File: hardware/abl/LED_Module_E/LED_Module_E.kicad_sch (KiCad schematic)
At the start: 90 parts, among them J1 SFW20S-2STE1LF, J3 009159008603906, Q1 Si3456DDV, Q11 Si3456DDV, Q12 Si3456DDV, Q2 Si3456DDV, Q3 Si3456DDV, Q4 Si3456DDV, Q5 Si3456DDV, Q6 Si3456DDV, Q7 Si3456DDV, Q8 Si3456DDV, U1 TMP1075DGK, U2 74HC245, U3 24AA025UIDT-I/OT

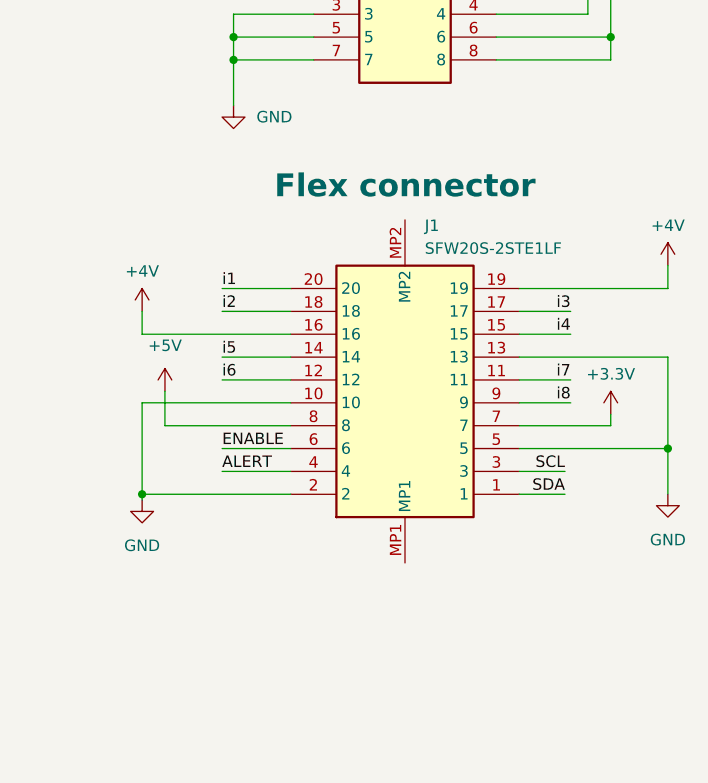
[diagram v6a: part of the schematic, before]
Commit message: Fix orientation of the flex connector.
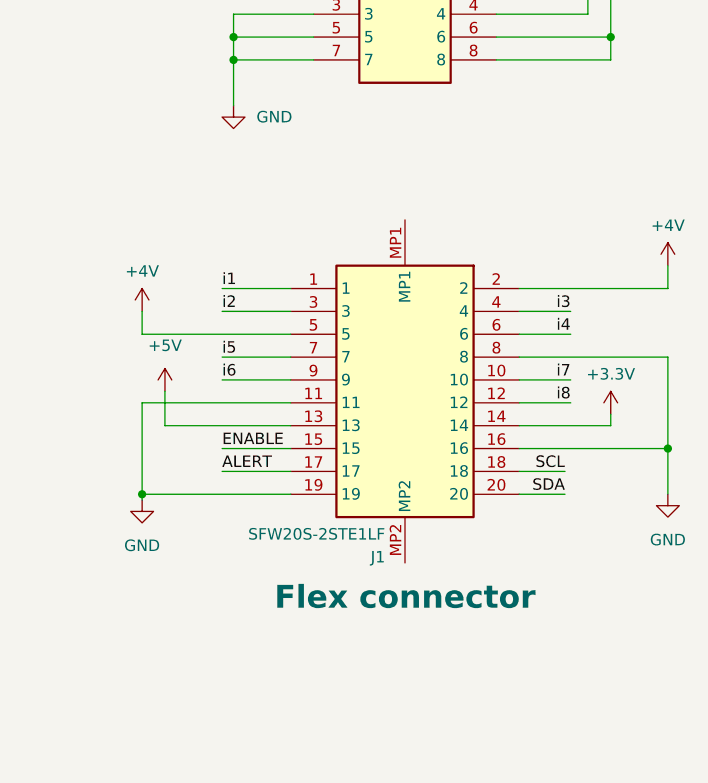
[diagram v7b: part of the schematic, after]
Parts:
- J1: footprint SFW20S2STE1LF -> Own footprints:SFW20S2STE1LF_Own
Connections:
- net +3.3V: now also J1.14; no longer J1.7
- net +4V: now also J1.2, J1.5; no longer J1.16, J1.19
- net +5V: now also J1.13; no longer J1.8
- net ALERT: now also J1.17; no longer J1.4
- net ENABLE: now also J1.15; no longer J1.6
- net GND: now also J1.11, J1.16, J1.19, J1.8; no longer J1.10, J1.13, J1.2, J1.5
- net SCL: now also J1.18; no longer J1.3
- net SDA: now also J1.20; no longer J1.1
- net i1: now also J1.1; no longer J1.20
- net i2: now also J1.3; no longer J1.18
- net i3: now also J1.4; no longer J1.17
- net i4: now also J1.6; no longer J1.15
- net i5: now also J1.7; no longer J1.14
- net i6: now also J1.9; no longer J1.12
- net i7: now also J1.10; no longer J1.11
- net i8: now also J1.12; no longer J1.9
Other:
- moved on the sheet: J1
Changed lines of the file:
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@@
 	(symbol
 		(lib_id "SFW20S-2STE1LF:SFW20S-2STE1LF")
-		(at 246.38 154.94 90)
+		(at 246.38 116.84 270)
 		(unit 1)
 		(exclude_from_sim no)
@@
 		(dnp no)
 		(property "Reference" "J1"
-			(at 248.5741 117.475 90)
+			(at 244.1859 154.305 90)
 			(effects
 				(font
@@
 		)
 		(property "Value" "SFW20S-2STE1LF"
-			(at 248.5741 120.015 90)
+			(at 244.1859 151.765 90)
 			(effects
 				(font
@@
 			)
 		)
-		(property "Footprint" "SFW20S2STE1LF"
-			(at 336.22 120.65 0)
+		(property "Footprint" "Own footprints:SFW20S2STE1LF_Own"
+			(at 156.54 151.13 0)
 			(effects
 				(font
@@
 		)
 		(property "Datasheet" "https://cdn.amphenol-cs.com/media/wysiwyg/files/drawing/10172832.pdf"
-			(at 436.22 120.65 0)
+			(at 56.54 151.13 0)
 			(effects
 				(font
@@
 		)
 		(property "Description" "1.00mm Flex Connector, SFW Straight series, 20 Position, Top Entry Surface Mount, ZIF"
-			(at 246.38 154.94 0)
+			(at 246.38 116.84 0)
 			(effects
 				(font
@@
 		)
 		(property "Manufacturer_Name" "Amphenol Communications Solutions"
-			(at 936.22 120.65 0)
+			(at -443.46 151.13 0)
 			(effects
 				(font
@@
 		)
 		(property "Manufacturer_Part_Number" "SFW20S-2STE1LF"
-			(at 1036.22 120.65 0)
+			(at -543.46 151.13 0)
 			(effects
 				(font
@@
 		)
 		(property "LCSC Part #" "C5407823"
-			(at 246.38 154.94 0)
+			(at 246.38 116.84 0)
 			(effects
 				(font
@@
 		)
 		(property "Purpose" "Flex connector"
-			(at 246.38 113.03 90)
+			(at 246.38 158.75 90)
 			(effects
 				(font
@@
 		)
 		(property "Note" ""
-			(at 246.38 154.94 0)
+			(at 246.38 116.84 0)
 			(effects
 				(font

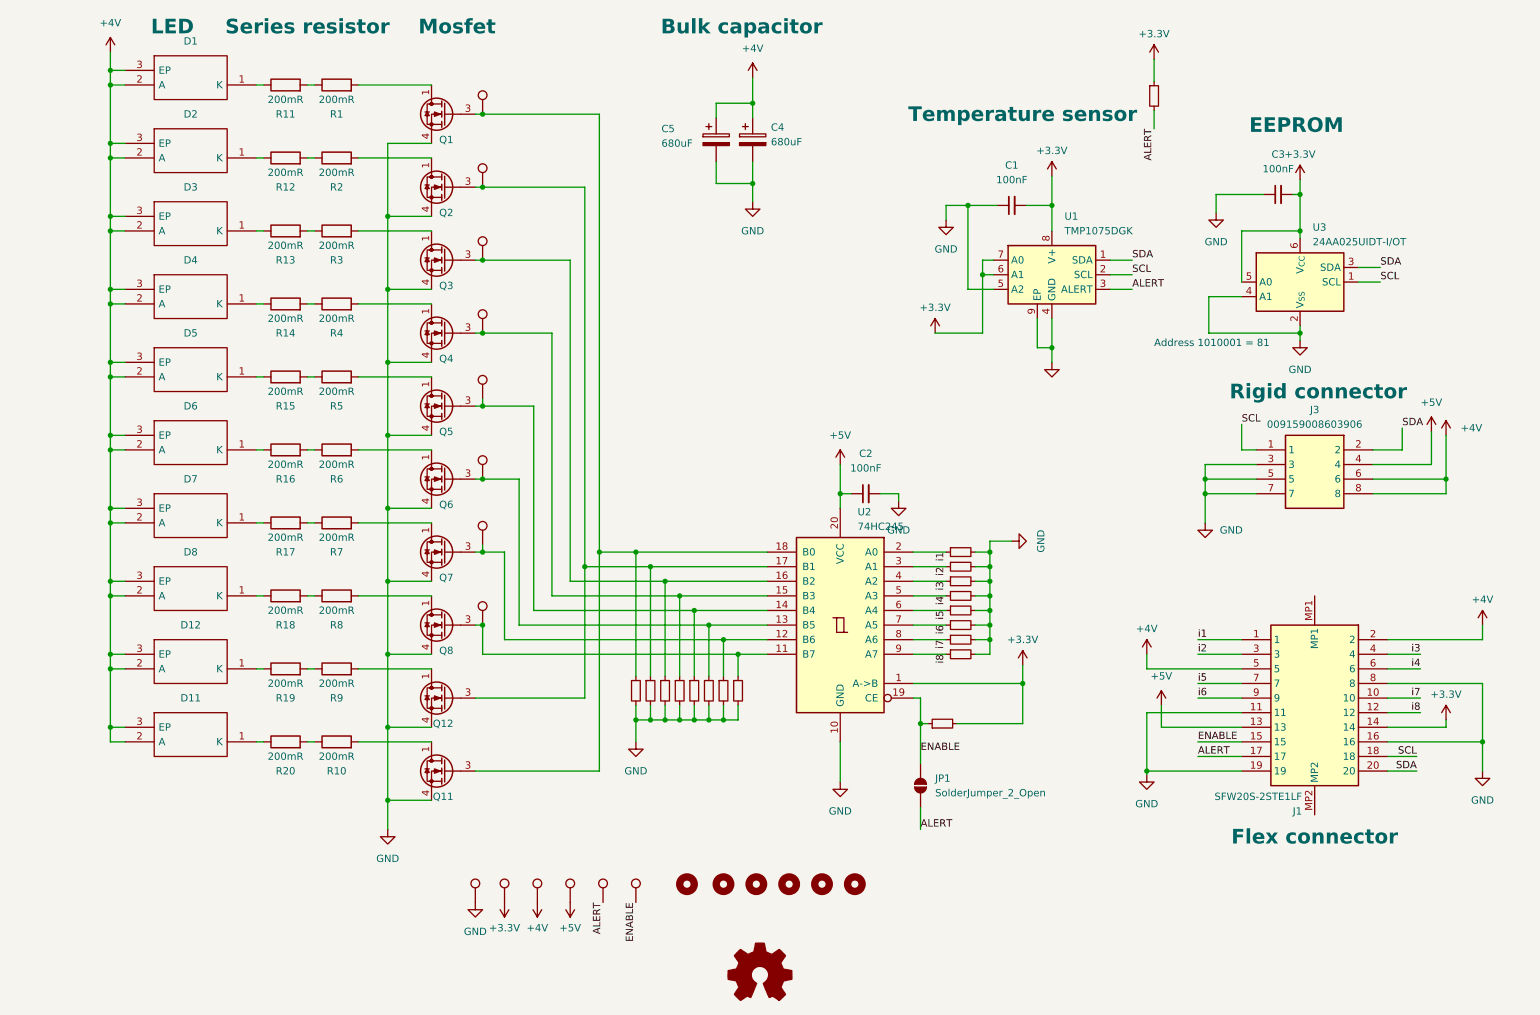
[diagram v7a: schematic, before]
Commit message: Add small copper PCB that only contains LEDs and temperature sensor.
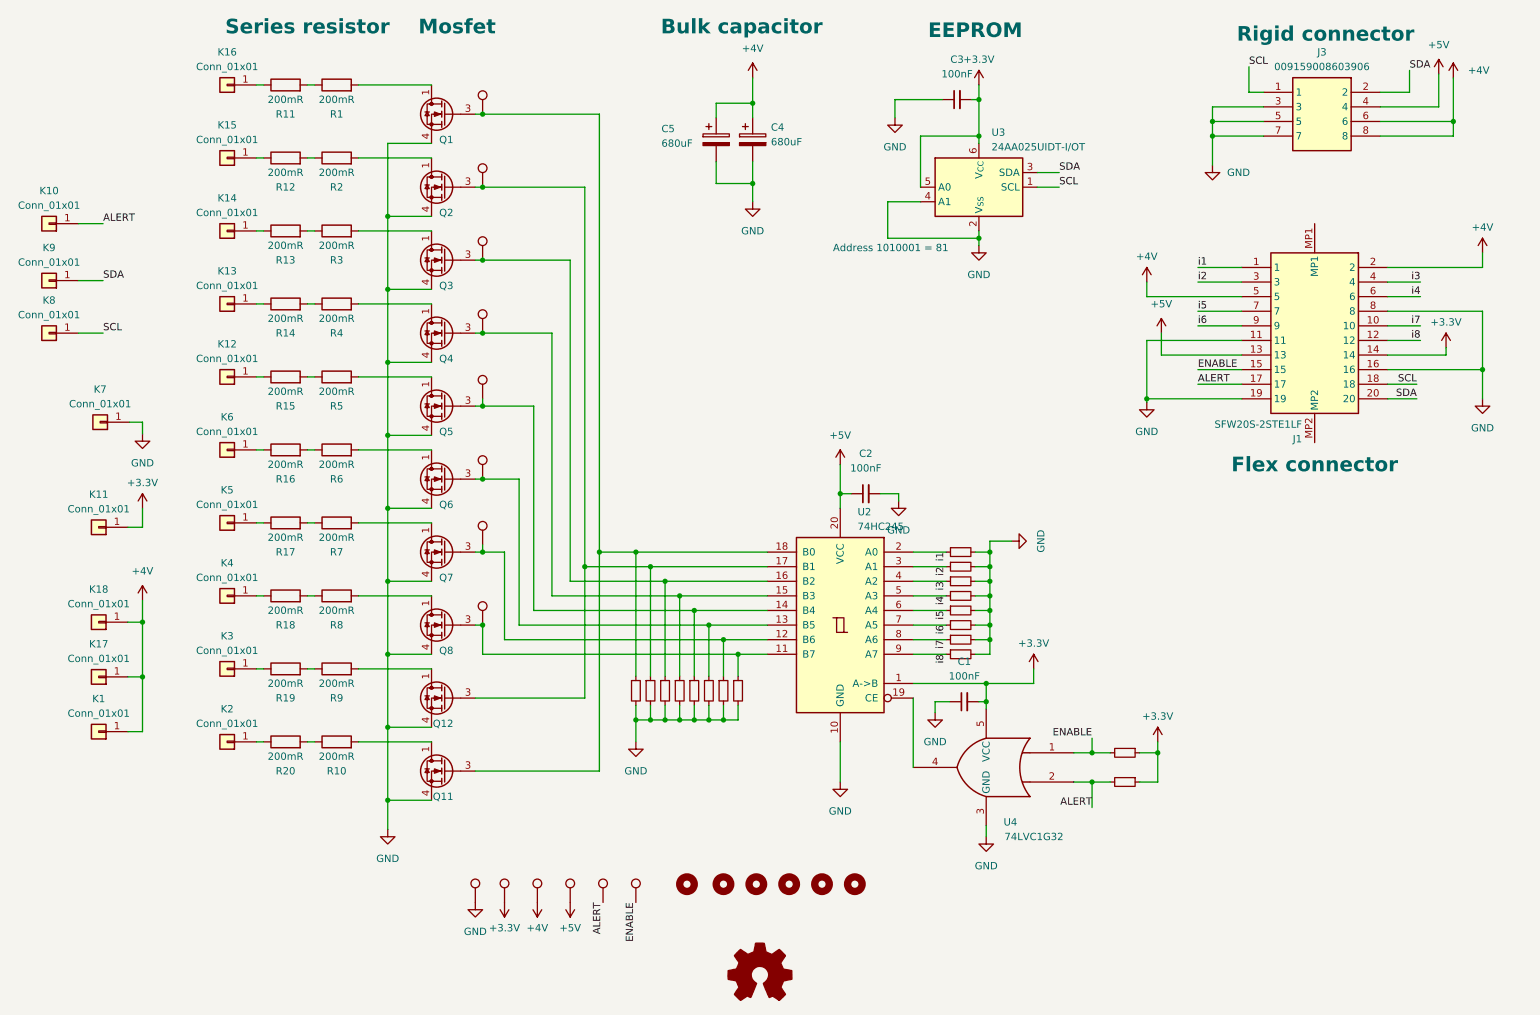
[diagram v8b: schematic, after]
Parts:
- removed D1, D11, D12, D2, D3, D4, D5, D6, D7, D8: XEGAVT-H0-0000-000-000000K2001, Cree XLAMP XE-G LED XEGAVT-H0:XEGAVTH_clean, symbol XEGAVT-H0-0000-000-000000K2001:XEGAVT-H0-0000-000-000000K2001
- removed JP1: SolderJumper_2_Open, Jumper:SolderJumper-2_P1.3mm_Open_TrianglePad1.0x1.5mm, symbol Jumper:SolderJumper_2_Open
- removed U1: TMP1075DGK, Package_SO:VSSOP-8_3.0x3.0mm_P0.65mm, symbol Sensor_Temperature:TMP1075DSG
- added K1, K10, K11, K12, K13, K14, K15, K16, K17, K18, K2, K3, K4, K5, K6, K7, K8, K9: Conn_01x01, TestPoint:TestPoint_THTPad_1.0x1.0mm_Drill0.5mm, symbol Connector_Generic:Conn_01x01
- added U4: 74LVC1G32, Package_TO_SOT_SMD:SOT-353_SC-70-5, symbol 74xGxx:74LVC1G32
- C1: In Stock 88 -> 19
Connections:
- net +3.3V: now also R41.1, K11.1 (Pin_1), U4.5 (VCC); no longer R41.2
- net +4V: now also K1.1 (Pin_1), K17.1 (Pin_1), K18.1 (Pin_1)
- net ALERT: now also K10.1 (Pin_1), U4.2
- net ENABLE: now also R41.2, U4.1; no longer R41.1, U2.19 (CE)
- net GND: now also K7.1 (Pin_1), U4.3 (GND)
- net SCL: now also K8.1 (Pin_1)
- net SDA: now also K9.1 (Pin_1)
- net at R18.1: now also K4.1 (Pin_1)
- net at R19.1: now also K3.1 (Pin_1)
- net at R16.1: now also K6.1 (Pin_1)
- net at R14.1: now also K13.1 (Pin_1)
- net at R17.1: now also K5.1 (Pin_1)
- net at R11.1: now also K16.1 (Pin_1)
- net at R15.1: now also K12.1 (Pin_1)
- net at R20.1: now also K2.1 (Pin_1)
- net at R12.1: now also K15.1 (Pin_1)
- net at R13.1: now also K14.1 (Pin_1)
- new net: U2.19 (CE), U4.4
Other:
- moved on the sheet: C3, J1, J3, U3
